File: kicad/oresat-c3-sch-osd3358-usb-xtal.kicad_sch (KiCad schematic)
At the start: 42 parts, among them J2 FTSH-105-XX-X-DV-K, U1 OSD3358-512M-BSM, U11 RCLAMP0504FB, U12 TPS2051CDBVR, Y1 24MHz, Y2 Crystal

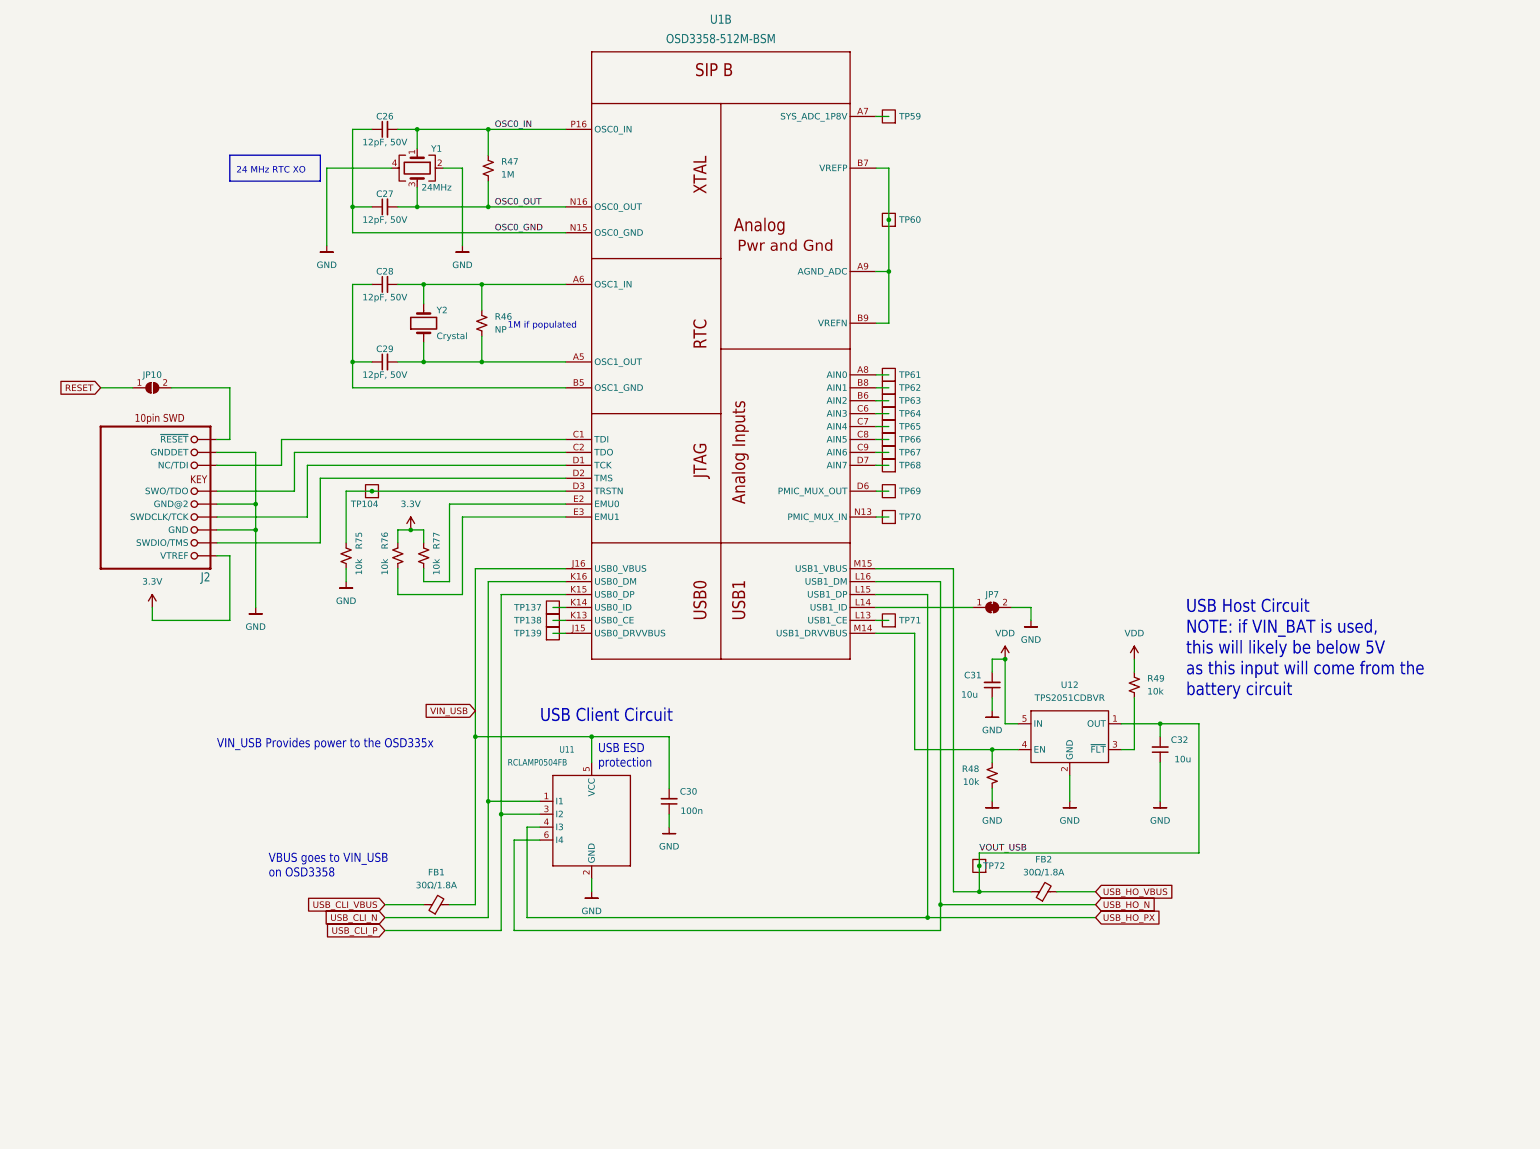
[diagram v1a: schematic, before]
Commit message: C3 v6 schematic now 80% done. OSD2258 IC has been gone over with a fine tooth comb and simplified as much as possible. OSD3358 pinout compared to RED board and PocketBeagle. What's left: lots of little issues, footprints, and then L band and UHF radio schematics need to be fixed.
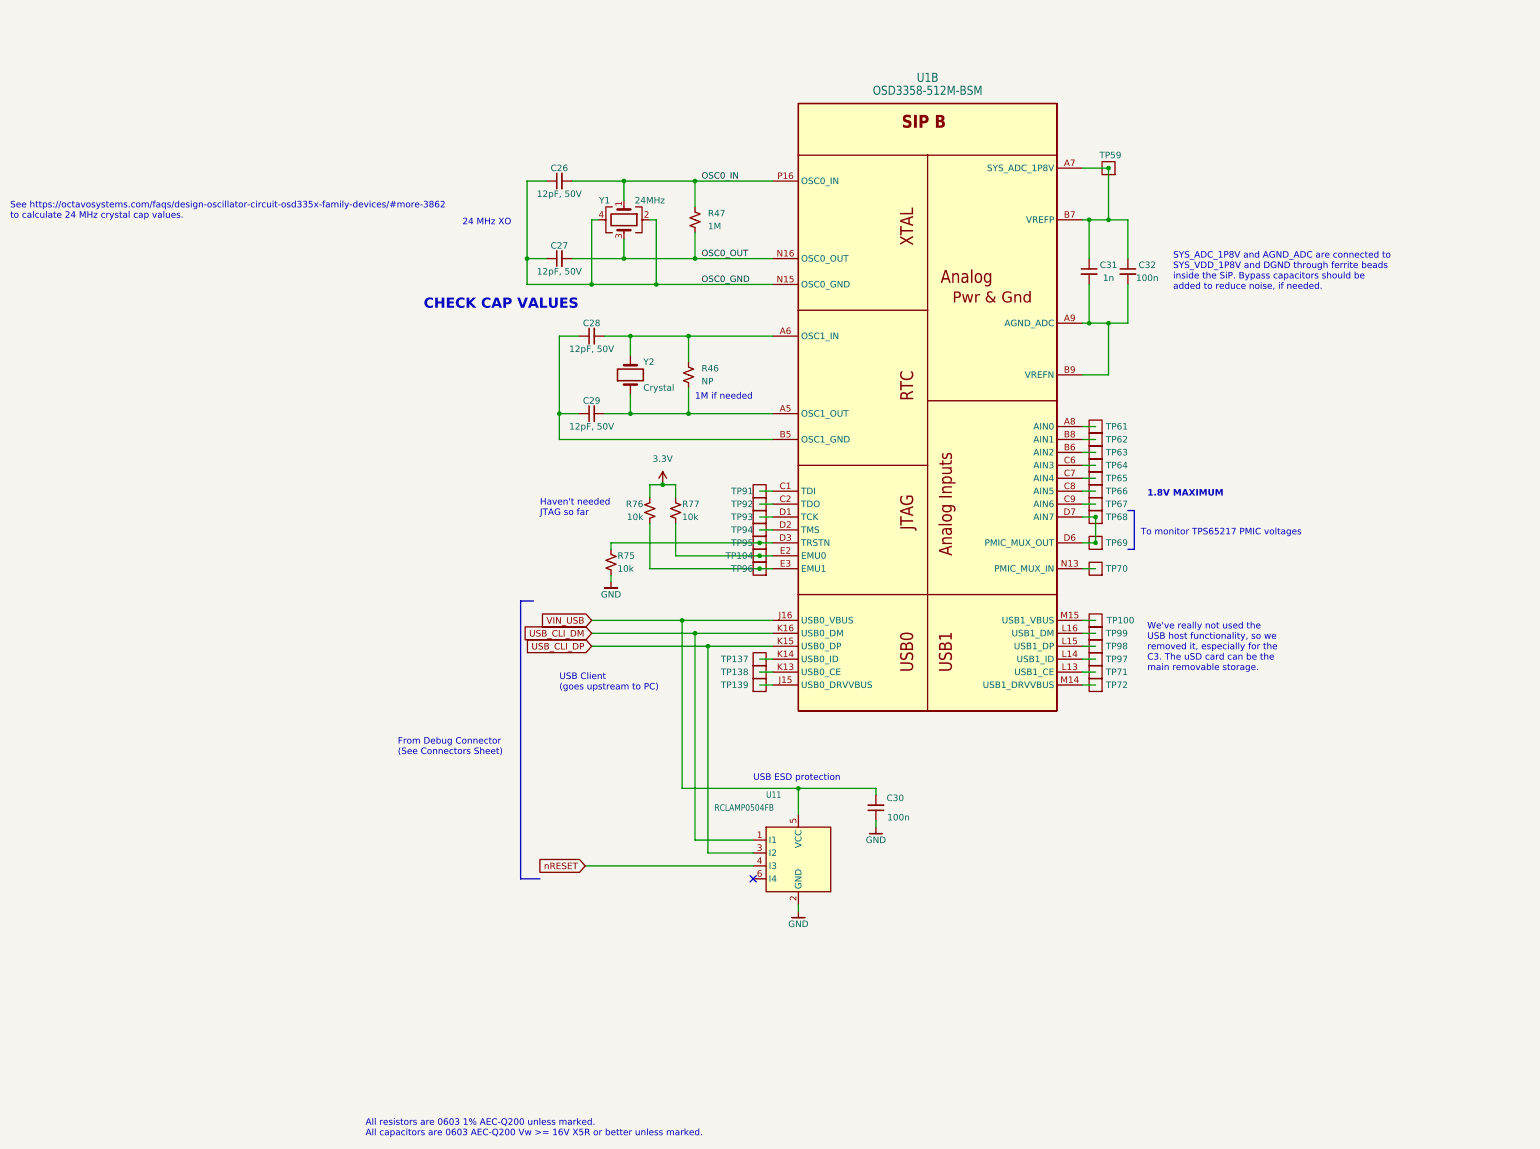
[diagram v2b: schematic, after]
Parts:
- removed FB1, FB2: 30Ω/1.8A, Inductor_SMD:L_0603_1608Metric, symbol Device:FerriteBead_Small
- removed J2: FTSH-105-XX-X-DV-K, oresat-footprints:J-Samtec-CON10_2X5_DUK_FTSH, symbol J-Samtec-FTSH-105-XX-X-DV-K-jtag-connector:FTSH-105-XX-X-DV-K
- removed JP10: SolderJumper_2_Open, oresat-footprints:SMT-JUMPER_2_NO_SILK, symbol Jumper:SolderJumper_2_Open
- removed JP7: SolderJumper_2_Bridged, oresat-footprints:SMT-JUMPER_2_NC_TRACE_SILK, symbol Jumper:SolderJumper_2_Bridged
- removed R48, R49: 10k, Resistor_SMD:R_0603_1608Metric, symbol Device:R_Small_US
- removed TP60: Test-Point, OreSat-TestPoint:PAD.03X.04, symbol OreSat-TestPoint:Test-Point
- removed U12: TPS2051CDBVR, Package_TO_SOT_SMD:SOT-23-5, symbol U-TI-TPS2051CDBVR-usb-power-switch:TPS2051CDBVR
- added TP100, TP91, TP92, TP93, TP94, TP95, TP96, TP97, TP98, TP99: Test-Point, OreSat-TestPoint:PAD.03X.04, symbol OreSat-TestPoint:Test-Point
- C31: value 10u -> 1n; footprint Capacitor_SMD:C_0805_2012Metric -> Capacitor_SMD:C_0603_1608Metric
- C32: value 10u -> 100n; footprint Capacitor_SMD:C_0805_2012Metric -> Capacitor_SMD:C_0603_1608Metric
- U1: symbol U-OSD3358-512M-BSM:OSD3358-512M-BSM -> oresat-ics:OSD3358-512M-BSM
- U11: symbol U-Semtech-RCLAMP0504FB-tvs-diodes:RCLAMP0504FB -> oresat-ics:RCLAMP0504FB
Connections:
- net VDD is gone; now on an unnamed net: C31.2
- net GND: no longer C31.1, C32.1, Y1.2, Y1.4
- net OSC0_GND: now also Y1.2, Y1.4
- net at U1.A9 (AGND_ADC), U1.B9 (VREFN): now also C32.2; no longer U1.B7 (VREFP)
- net at U1.D2 (TMS): now also TP94.1
- net at U1.D1 (TCK): now also TP93.1
- net at U1.C2 (TDO): now also TP92.1
- net at U1.C1 (TDI): now also TP91.1
- net at R76.2, U1.E3 (EMU1): now also TP96.1
- net at U1.L14 (USB1_ID): now also TP97.1
- net at TP69.1, U1.D6 (PMIC_MUX_OUT): now also TP68.1, U1.D7 (AIN7)
- net at U1.M14 (USB1_DRVVBUS): now also TP72.1
- net at TP59.1, U1.A7 (SYS_ADC_1P8V): now also C31.1, C32.1, U1.B7 (VREFP)
- net at R77.2, U1.E2 (EMU0): now also TP95.1
- net USB_CLI_N renamed USB_CLI_DM
- net USB_CLI_P renamed USB_CLI_DP
- net USB_HO_N: no longer names the net of U11.6 (I4)
- net USB_HO_N: no longer U1.L16 (USB1_DM)
- net USB_HO_PX: no longer names the net of U1.L15 (USB1_DP)
- net USB_HO_PX: now also TP98.1; no longer U11.4 (I3)
- removed net VOUT_USB: C32.2, TP72.1, U1.M15 (USB1_VBUS)
- new net: TP100.1, U1.M15 (USB1_VBUS)
- new net: TP99.1, U1.L16 (USB1_DM)
- new net nRESET: U11.4 (I3)
- no-connect marks 0 -> 1
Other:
- note added: "1.8V MAXIMUM"
- note added: "1M if needed"
- note added: "24 MHz XO"
- note added: "All resistors are 0603 1% AEC-Q200 unless marked. All capacitors are 0603 AEC-Q200 Vw >= 16V X5R or better unless marked."
- note added: "CHECK CAP VALUES"
- note added: "From Debug Connector (See Connectors Sheet)"
- note added: "Haven't needed JTAG so far"
- note added: "SYS_ADC_1P8V and AGND_ADC are connected to SYS_VDD_1P8V and DGND through ferrite beads inside the SiP. Bypass capacitors should be added to reduce noise, if needed."
- note added: "See https://octavosystems.com/faqs/design-oscillator-circuit-osd335x-family-devices/#more-3862 to calculate 24 MHz crystal cap values."
- note added: "To monitor TPS65217 PMIC voltages"
- note added: "USB Client (goes upstream to PC)"
- note added: "We've really not used the USB host functionality, so we removed it, especially for the C3. The uSD card can be the main removable storage."
- note removed: "1M if populated"
- note removed: "24 MHz RTC XO"
- note removed: "USB Client Circuit"
- note removed: "USB Host Circuit NOTE: if VIN_BAT is used, this will likely be below 5V as this input will come from the battery circuit"
- note removed: "VBUS goes to VIN_USB on OSD3358"
- note removed: "VIN_USB Provides power to the OSD335x"
- title: (none) -> OreSat C3: OSD3358 SIP B
- moved on the sheet: C26, C27, C28, C29, C30, R46, R47, R75, R76, R77, TP104, TP137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

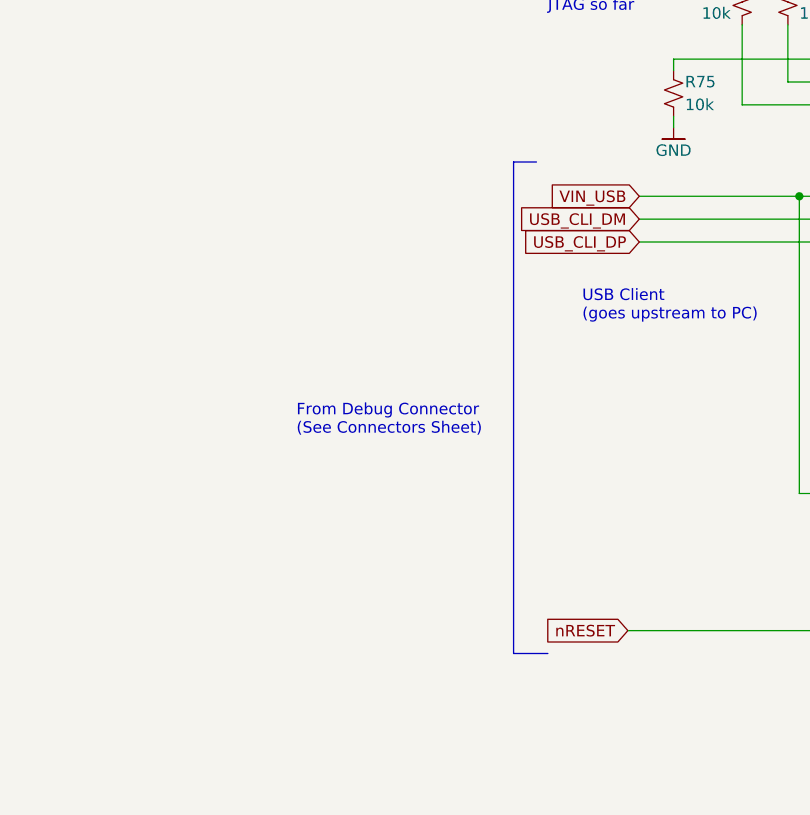
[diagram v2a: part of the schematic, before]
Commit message: Finished UHF radio schematic. Added sheet numbers to external labels. Still to do: L band radio, hooking up GPIO to the OSD3358, and test points.
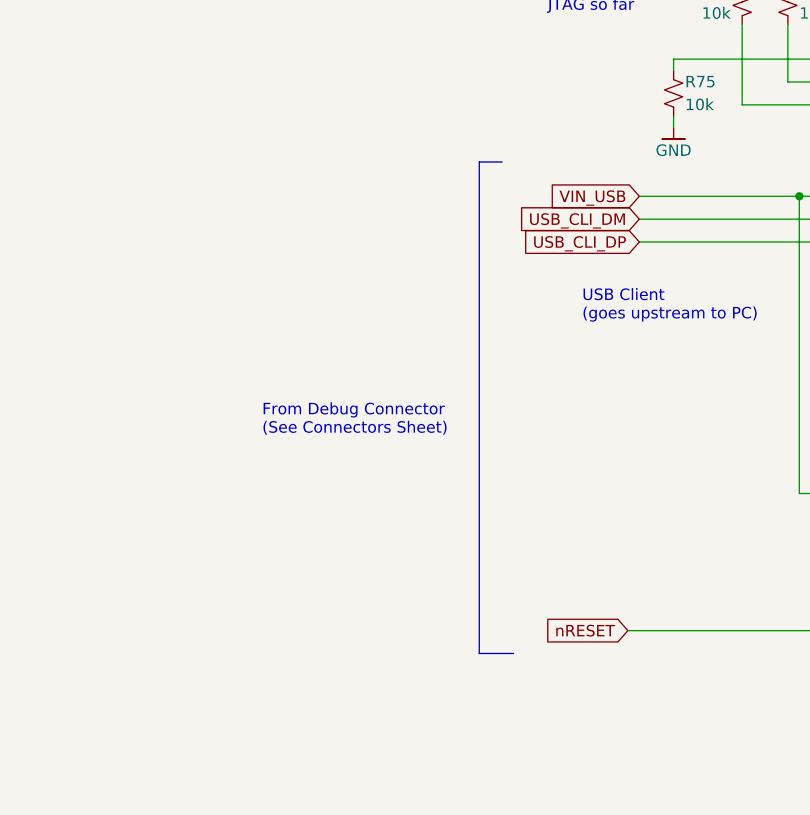
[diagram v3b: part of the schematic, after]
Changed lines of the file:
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@@
     (stroke (width 0) (type default))
   )
-  (polyline (pts (xy 146.05 156.21) (xy 146.05 210.82))
+  (polyline (pts (xy 142.24 156.21) (xy 142.24 210.82))
     (stroke (width 0) (type default))
   )
@@
     (stroke (width 0) (type default))
   )
-  (polyline (pts (xy 148.59 156.21) (xy 146.05 156.21))
+  (polyline (pts (xy 144.78 156.21) (xy 142.24 156.21))
     (stroke (width 0) (type default))
   )
@@
     (stroke (width 0) (type default))
   )
-  (polyline (pts (xy 146.05 210.82) (xy 149.86 210.82))
+  (polyline (pts (xy 142.24 210.82) (xy 146.05 210.82))
     (stroke (width 0) (type default))
   )
@@
     (effects (font (size 1.27 1.27)) (justify left bottom))
   )
-  (text "From Debug Connector\n(See Connectors Sheet)" (at 121.92 186.69 0)
+  (text "From Debug Connector\n(See Connectors Sheet)" (at 118.11 186.69 0)
     (effects (font (size 1.27 1.27)) (justify left bottom))
   )
@@
     (effects (font (size 1.2446 1.2446)) (justify left bottom))
   )
-  (global_label "USB_CLI_DP" (shape input) (at 160.02 165.1 180) (fields_autoplaced)
+  (global_label "USB_CLI_DP" (shape input) (at 160.02 165.1 180)
     (effects (font (size 1.27 1.27)) (justify right))
-    (property "Intersheetrefs" "${INTERSHEET_REFS}" (at 145.9261 165.1 0)
-      (effects (font (size 1.27 1.27)) (justify right) hide)
+    (property "Intersheetrefs" "${INTERSHEET_REFS}" (at 146.05 165.1 0)
+      (effects (font (size 1.27 1.27)) (justify right))
     )
   )
-  (global_label "nRESET" (shape input) (at 158.75 208.28 180) (fields_autoplaced)
+  (global_label "nRESET" (shape input) (at 158.75 208.28 180)
     (effects (font (size 1.27 1.27)) (justify right))
-    (property "Intersheetrefs" "${INTERSHEET_REFS}" (at 148.9501 208.28 0)
-      (effects (font (size 1.27 1.27)) (justify right) hide)
+    (property "Intersheetrefs" "${INTERSHEET_REFS}" (at 148.59 208.28 0)
+      (effects (font (size 1.27 1.27)) (justify right))
     )
   )
-  (global_label "USB_CLI_DM" (shape input) (at 160.02 162.56 180) (fields_autoplaced)
+  (global_label "USB_CLI_DM" (shape input) (at 160.02 162.56 180)
     (effects (font (size 1.27 1.27)) (justify right))
-    (property "Intersheetrefs" "${INTERSHEET_REFS}" (at 145.7447 162.56 0)
-      (effects (font (size 1.27 1.27)) (justify right) hide)
+    (property "Intersheetrefs" "${INTERSHEET_REFS}" (at 146.05 162.56 0)
+      (effects (font (size 1.27 1.27)) (justify right))
     )
   )
@@
     (effects (font (size 1.27 1.27)) (justify right))
     (property "Intersheetrefs" "${INTERSHEET_REFS}" (at 149.8055 159.9406 0)
-      (effects (font (size 1.27 1.27)) (justify right) hide)
+      (effects (font (size 1.27 1.27)) (justify right))
     )
   )

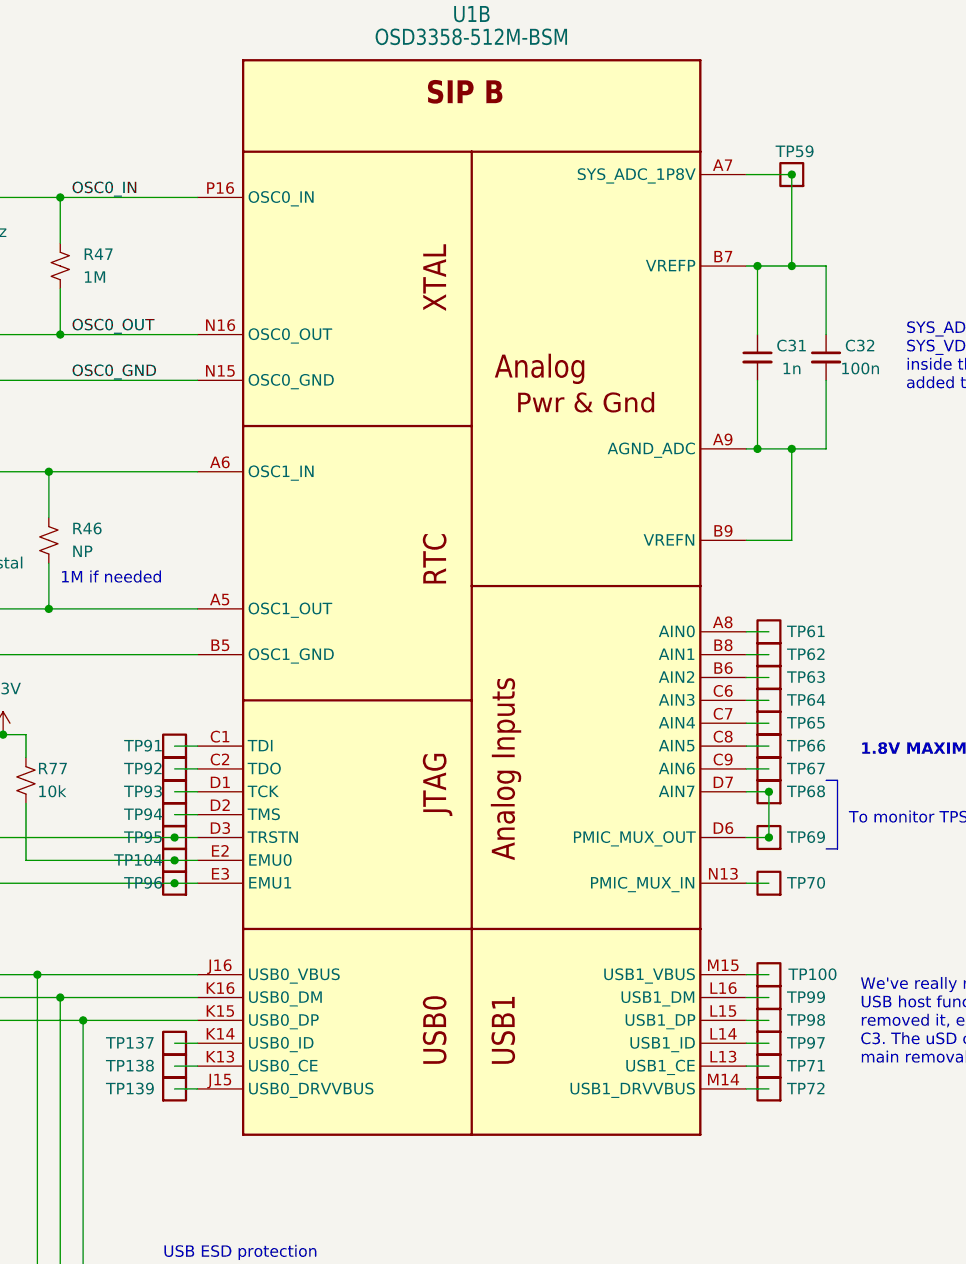
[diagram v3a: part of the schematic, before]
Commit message: Sane amount of ERC errors now; mostly library cleanups.
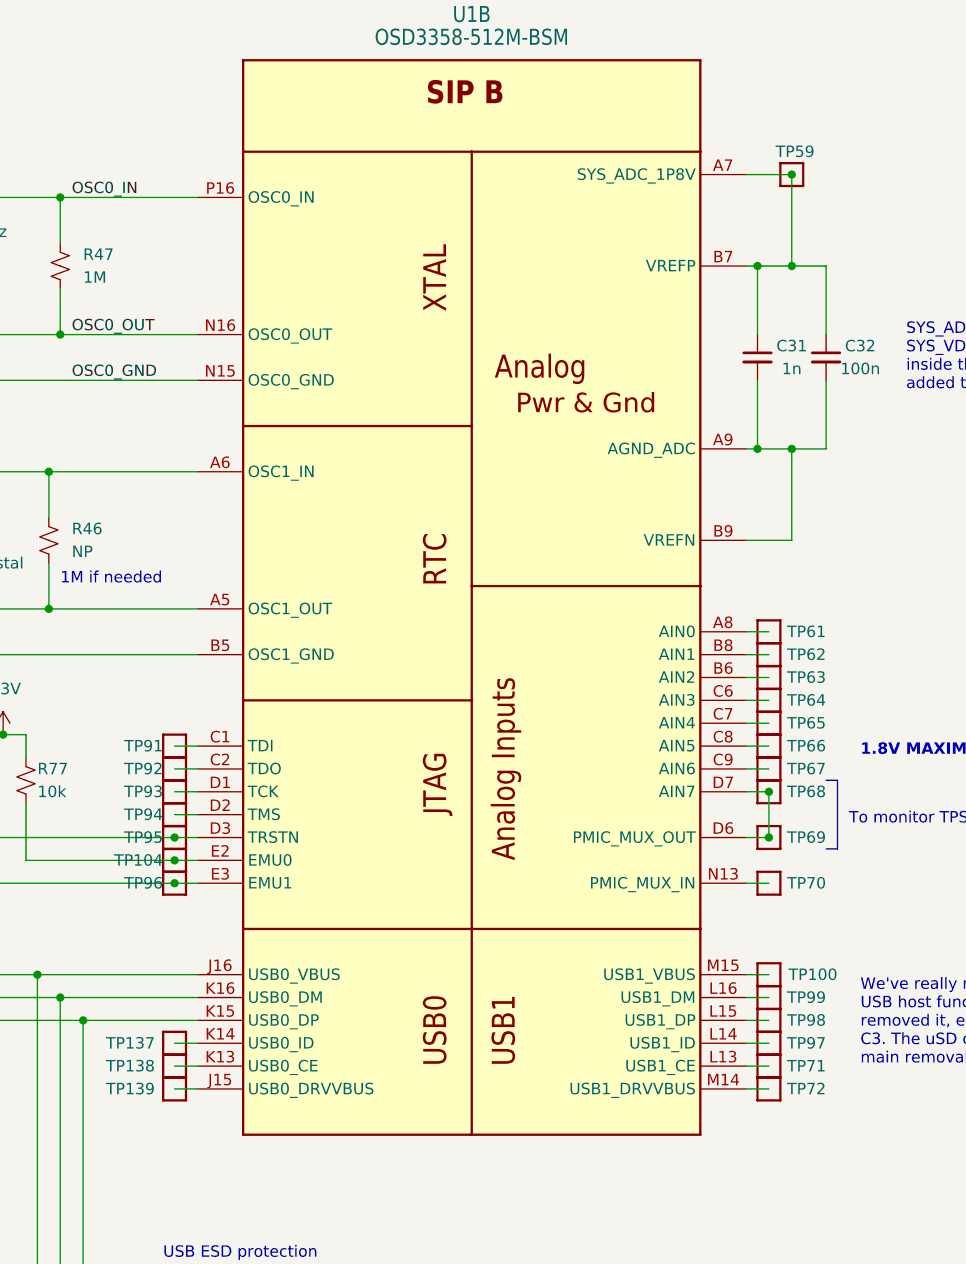
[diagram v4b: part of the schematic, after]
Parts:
- TP100, TP104, TP137, TP138, TP139, TP59, TP61, TP62, TP63, TP64, TP65, TP66, TP67, TP68, TP69, TP70, TP71, TP72, TP91, TP92, TP93, TP94, TP95, TP96, TP97, TP98, TP99: footprint OreSat-TestPoint:PAD.03X.04 -> oresat-misc:PAD.03X.04; symbol OreSat-TestPoint:Test-Point -> oresat-misc:Test-Point
